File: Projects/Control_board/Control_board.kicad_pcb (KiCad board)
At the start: 2 copper layers, 97.1 x 121.5 mm, 47 parts, among them IC2 PCA9615DPJ, J1 5055780871, J2 43045-0200, J3 43045-0200, J4 43045-0200, J5 43045-0401, J6 RJ45, J8 Conn_01x02, K3 PB114024, Q1 BSS138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

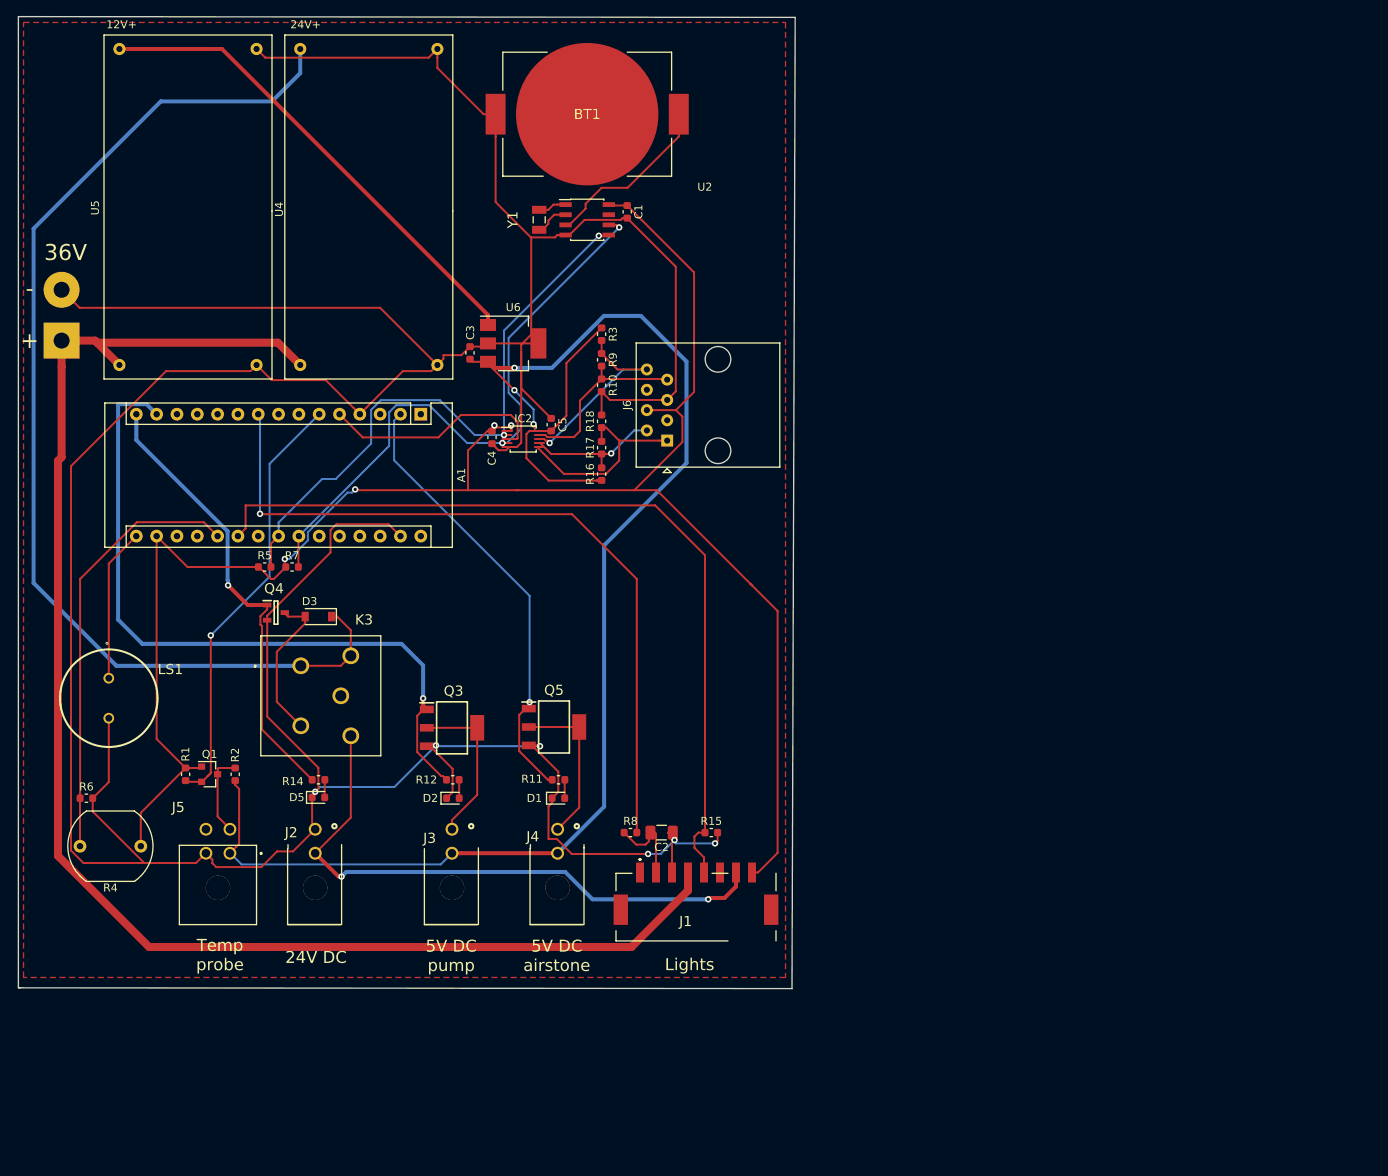
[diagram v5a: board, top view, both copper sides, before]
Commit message: new LED board IS3117... plus sorted out libraries
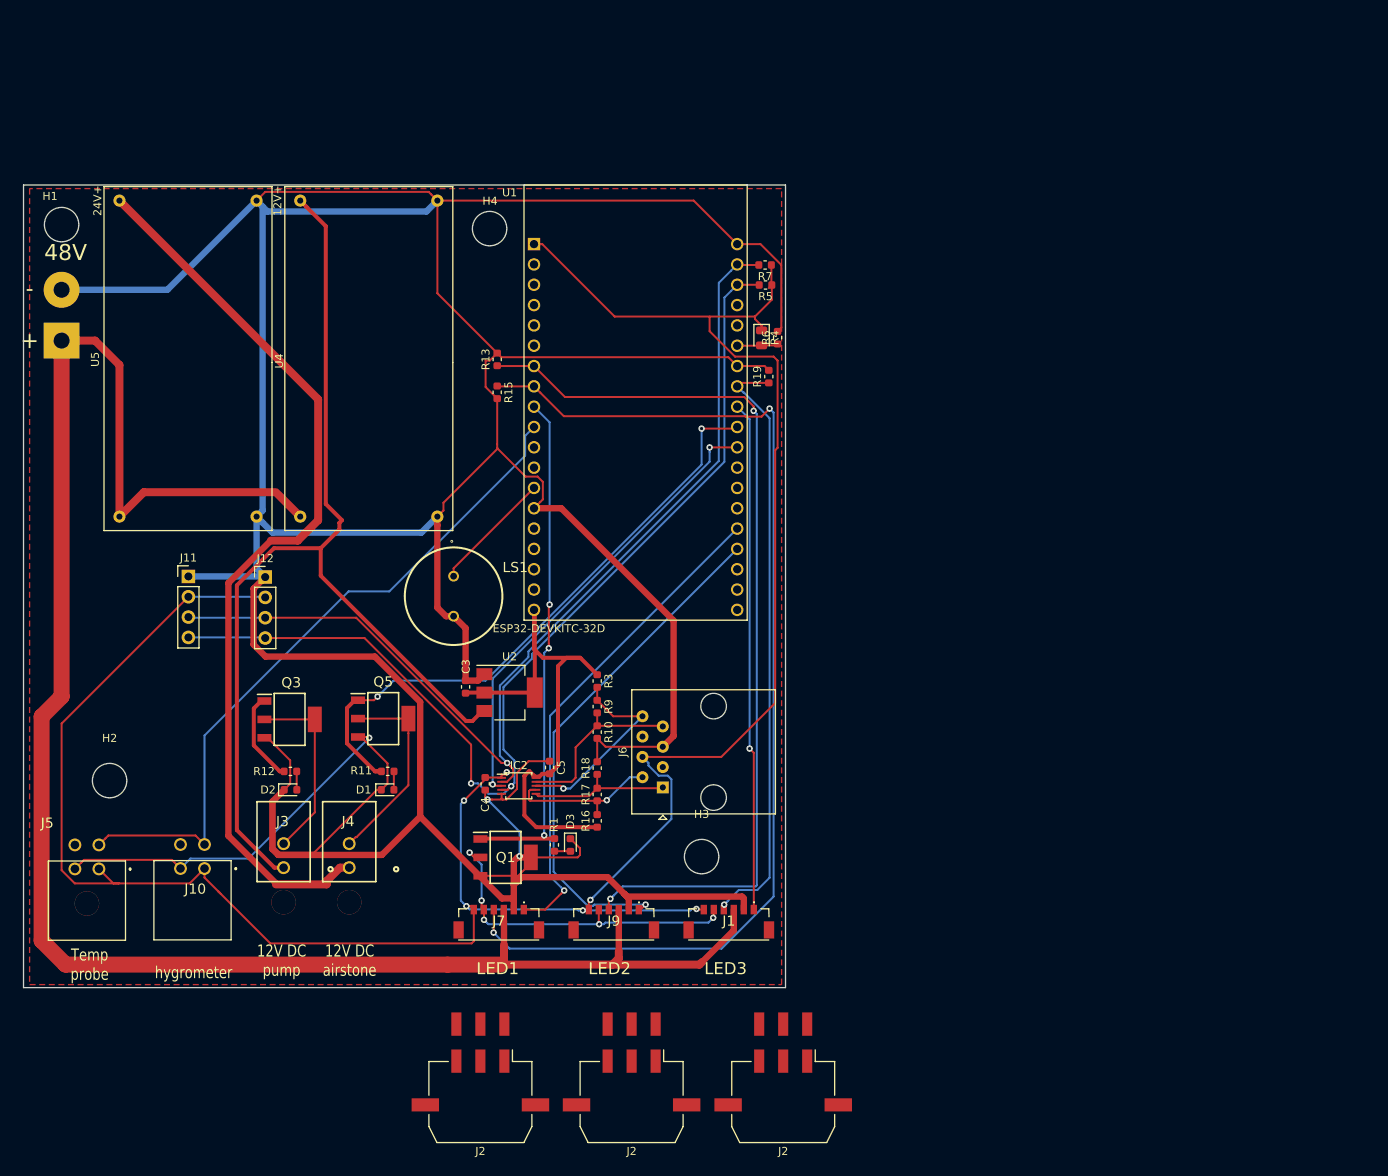
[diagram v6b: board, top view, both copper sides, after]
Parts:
- removed A1: Arduino_Nano_v2.x, Module:Arduino_Nano
- removed BT1: Battery_Cell, SamacSys_Parts:BATHLD001
- removed C1: 0.1uF, Capacitor_SMD:C_0603_1608Metric
- removed C2: 1uF, Capacitor_SMD:C_1206_3216Metric
- removed D5: LED, LED_SMD:LED_0603_1608Metric
- removed the J2 at (115.2, 170.4)
- removed K3: PB114024, SamacSys_Parts:PB114024
- removed Q4: PDTD113ET,215, SamacSys_Parts:SOT95P230X110-3N
- removed R14: 1k, Resistor_SMD:R_0603_1608Metric
- removed R2: 10k, Resistor_SMD:R_0603_1608Metric
- removed R8: 10K, Resistor_SMD:R_0603_1608Metric
- removed U6: TC1262-50, Package_TO_SOT_SMD:SOT-223-3_TabPin2
- removed Y1: Crystal, SamacSys_Parts:FC135327680KAAG0
- added H1: MountingHole, MountingHole:MountingHole_4.3mm_M4, F.Cu at (83.5, 87.5)
- added H2: MountingHole, MountingHole:MountingHole_4.3mm_M4, F.Cu at (89.5, 157.0)
- added H3: MountingHole, MountingHole:MountingHole_4.3mm_M4, F.Cu at (163.5, 166.5)
- added H4: MountingHole, MountingHole:MountingHole_4.3mm_M4, F.Cu at (137.0, 88.0)
- added J10: 43045-0401, SamacSys_Parts:430450401, F.Cu at (100.2, 170.9)
- added J11: Conn_01x04, Connector_PinHeader_2.54mm:PinHeader_1x04_P2.54mm_Vertical, F.Cu at (99.3, 131.5)
- added J12: Conn_01x04, Connector_PinHeader_2.54mm:PinHeader_1x04_P2.54mm_Vertical, F.Cu at (109.0, 131.6)
- added J2: 43045-0609, Connector_Molex:Molex_Micro-Fit_3.0_43045-0610_2x03-1MP_P3.00mm_Horizontal, F.Cu at (173.7, 189.8)
- added J2: 43045-0609, Connector_Molex:Molex_Micro-Fit_3.0_43045-0610_2x03-1MP_P3.00mm_Horizontal, F.Cu at (154.8, 189.8)
- added J2: 43045-0609, Connector_Molex:Molex_Micro-Fit_3.0_43045-0610_2x03-1MP_P3.00mm_Horizontal, F.Cu at (135.8, 189.8)
- added J7: 505567-0681, SamacSys_Parts:5055670681, F.Cu at (138.2, 174.6)
- added J9: 505567-0681, SamacSys_Parts:5055670681, F.Cu at (152.5, 174.6)
- added R13: 10K, Resistor_SMD:R_0603_1608Metric, F.Cu at (137.9, 104.3)
- added R19: 10K, Resistor_SMD:R_0603_1608Metric, F.Cu at (171.9, 106.5)
- added U1: ESP32-DEVKITC-32D, ESP32-DEVKITC-32D:MODULE_ESP32-DEVKITC-32D, F.Cu at (155.2, 109.7)
- D3: value MBR0520 -> LED; footprint Diode_SMD:D_SOD-123 -> LED_SMD:LED_0603_1608Metric
- J1: value 5055780871 -> 505567-0681; footprint footprints:5055780871 -> SamacSys_Parts:5055670681
- J3, J4: footprint Kicad_mylib:Molex_43045-0200 -> 43045-0200
- Q1: value BSS138 -> BSP75N; footprint Package_TO_SOT_SMD:SOT-23 -> SOT230P700X180-4N
- R1: value 10k -> 1k
- R4: footprint OptoDevice:R_LDR_10x8.5mm_P7.6mm_Vertical -> LED_SMD:LED_0805_2012Metric
- U2: value DS1307Z+ -> NCP1117-5.0_SOT223; footprint Package_SO:SOIC-8_3.9x4.9mm_P1.27mm -> Package_TO_SOT_SMD:SOT-223-3_TabPin2
- moved R6 103.8 mm to (173.0, 101.6), turned to 90 degrees
- moved R4 100.3 mm to (171.0, 101.7), turned to 270 degrees
- moved R5 71.8 mm to (171.5, 95.0), turned to 180 degrees
- moved R7 70.1 mm to (171.4, 92.5), turned to 180 degrees
- moved R15 61.2 mm to (137.9, 108.5), turned to 270 degrees
- moved U2 59.9 mm to (139.5, 146.0)
- moved R1 46.9 mm to (145.1, 165.0)
- moved LS1 44.9 mm to (132.5, 133.9)
- moved IC2 43.4 mm to (140.7, 157.7)
- moved R17 43.4 mm to (150.4, 158.7)
- moved R3 43.4 mm to (150.4, 144.6)
- moved J6 43.4 mm to (158.7, 157.8)
- moved R10 43.4 mm to (150.4, 150.9)
- moved R16 43.4 mm to (150.4, 162.0)
- moved R18 43.4 mm to (150.4, 155.4)
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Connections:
- D3 pad 1: +24V -> GND
- IC2 pad 2: Net-(A1-Pad23) -> /SDA
- IC2 pad 4: Net-(A1-Pad24) -> /SCL
- J1 pad 1: (no net) -> /ADJ_LED1
- J1 pad 2: /ADJ_LED -> GND
- J1 pad 3: GND -> +48V
- J1 pad 4: +36V -> /NTC_1
- J1 pad 5: /NTC -> /48V_Fan
- J1 pad 6: (no net) -> +3V3
- J1 pad 7: /12V_Fan -> (no net)
- J1 pad 8: +3V3 -> (no net)
- J3 pad 1: +5V -> +12V
- J4 pad 1: +5V -> +24V
- J5 pad 1: +5V -> +3V3
- J5 pad 3: /temp_data_5V -> /1-Wire
- J8 pad 1: +36V -> +48V
- LS1 pad 1: Net-(A1-Pad16) -> /buzzer
- Q1 pad 1: +3V3 -> /fan
- Q1 pad 2: /Temp_data_3V3 -> /48V_Fan
- Q1 pad 3: /temp_data_5V -> GND
- R1 pad 1: +3V3 -> /fan
- R1 pad 2: /Temp_data_3V3 -> Net-(D3-Pad2)
- R15 pad 1: /NTC -> /NTC_2
- R5 pad 2: Net-(A1-Pad23) -> /SCL
- R7 pad 2: Net-(A1-Pad24) -> /SDA
- U2 pad 1: Net-(U2-Pad1) -> GND
- U2 pad 2: Net-(U2-Pad2) -> +5V
- U2 pad 3: Net-(BT1-Pad1) -> +12V
- U4 pad 1: +36V -> +48V
- U4 pad 4: +24V -> +12V
- U5 pad 1: +36V -> +48V
- U5 pad 4: +12V -> +24V
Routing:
- net +48V: track 0.00 -> 239.2 mm
- net +36V: track 188.3 -> 0.00 mm
- net /NTC_2: track 0.00 -> 138.9 mm, vias 0 -> 2
- net GND: track 509.0 -> 642.1 mm, vias 6 -> 3
- net /SCL: track 0.00 -> 131.4 mm, vias 0 -> 2
- net /SDA: track 0.00 -> 128.8 mm, vias 0 -> 1
- net +5V: track 195.9 -> 69.2 mm, vias 3 -> 0
- net /NTC_3: track 0.00 -> 114.6 mm, vias 0 -> 2
- net /NTC: track 105.4 -> 0.00 mm
- net /ADJ: track 94.7 -> 0.00 mm, vias 1 -> 0
- net /1-Wire: track 0.00 -> 86.4 mm
- net /pump: track 89.6 -> 11.5 mm, vias 1 -> 0
- net Net-(A1-Pad24): track 77.7 -> 0.00 mm, vias 2 -> 0
- net Net-(A1-Pad23): track 76.8 -> 0.00 mm, vias 2 -> 0
- net +3V3: track 234.2 -> 310.2 mm, vias 4 -> 6
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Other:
- board size 97.1 x 121.5 mm -> 95.3 x 100.3 mm
- net class 36volt removed
- net class 48volt added: clearance 0.4, trace_width 1, via_dia 0.8, via_drill 0.4
- net class Power: trace_width 1 -> 0.8
- board text added: "12V DC airstone"
- board text added: "12V DC pump"
- board text added: "48V"
- board text added: "LED1"
- board text added: "LED2"
- board text added: "LED3"
- board text added: "hygrometer"
- board text removed: "24V DC"
- board text removed: "36V"
- board text removed: "5V DC airstone"
- board text removed: "5V DC pump"
- board text removed: "Lights"

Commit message: files after harddrive restore
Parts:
- removed the J2 at (173.7, 189.8)
- removed the J2 at (154.8, 189.8)
- removed the J2 at (135.8, 189.8)
- removed J9: 505567-0681, SamacSys_Parts:5055670681
- removed U5: DCDC_lm2596, Kicad_mylib:LM2596_module
- added C1: 100nF, Capacitor_SMD:C_0603_1608Metric, F.Cu at (137.0, 154.0)
- added C2: 100nF, Capacitor_SMD:C_0603_1608Metric, F.Cu at (151.2, 154.0)
- added C6: 100nF, Capacitor_SMD:C_0603_1608Metric, F.Cu at (166.2, 153.8)
- added C7: 100nF, Capacitor_SMD:C_0603_1608Metric, F.Cu at (174.0, 124.2)
- added D4: SMF5.0A, Diode_SMD:D_SOD-123F, F.Cu at (161.6, 157.2)
- added D5: SMF5.0A, Diode_SMD:D_SOD-123F, F.Cu at (146.2, 157.2)
- added D6: SMF5.0A, Diode_SMD:D_SOD-123F, F.Cu at (132.0, 157.2)
- added D7: SMF5.0A, Diode_SMD:D_SOD-123F, F.Cu at (137.4, 157.2)
- added D8: SMF5.0A, Diode_SMD:D_SOD-123F, F.Cu at (151.4, 157.2)
- added D9: SMF5.0A, Diode_SMD:D_SOD-123F, F.Cu at (166.6, 157.2)
- added IC1: VN7050ASTR, SamacSys_Parts:SOIC127P600X175-8N, F.Cu at (134.0, 146.5)
- added IC3: PSSI2021SAY,115, SamacSys_Parts:SOT65P210X100-5N, F.Cu at (100.0, 154.5)
- added J13: Conn_01x01_Female, Connector_PinHeader_1.00mm:PinHeader_1x01_P1.00mm_Horizontal, F.Cu at (170.8, 120.5)
- added J2: 66200621022, SamacSys_Parts:66200621022, F.Cu at (153.0, 167.8)
- added Q2: BSS138-Transistor_FET, Package_TO_SOT_SMD:SOT-23, F.Cu at (136.6, 125.4)
- added R14: 100, Resistor_SMD:R_0603_1608Metric, F.Cu at (151.2, 151.0)
- added R2: 10K, Resistor_SMD:R_0603_1608Metric, F.Cu at (136.8, 121.6)
- added R20: 100, Resistor_SMD:R_0603_1608Metric, F.Cu at (166.2, 151.0)
- added R21: 100, Resistor_SMD:R_0603_1608Metric, F.Cu at (171.0, 124.2)
- added R22: 4.7k, Resistor_SMD:R_0603_1608Metric, F.Cu at (98.5, 150.8)
- added R23: 15k, Resistor_SMD:R_0603_1608Metric, F.Cu at (138.0, 142.8)
- added R24: 39k, Resistor_SMD:R_0603_1608Metric, F.Cu at (96.2, 154.5)
- added R25: 10k, Resistor_SMD:R_0603_1608Metric, F.Cu at (102.8, 154.5)
- added R8: 100, Resistor_SMD:R_0603_1608Metric, F.Cu at (137.0, 151.0)
- J1, J7: value 505567-0681 -> 66200621022; footprint SamacSys_Parts:5055670681 -> SamacSys_Parts:66200621022
- J3, J4: footprint 43045-0200 -> footprints:43045-0200
- Q1: value BSP75N -> Q_NMOS_GSD; footprint SOT230P700X180-4N -> Package_TO_SOT_SMD:SOT-23
- moved J6 81.4 mm to (103.8, 97.6), turned to 180 degrees
- moved R3 71.3 mm to (90.5, 105.8), turned to 0 degrees
- moved R9 70.5 mm to (93.8, 105.8), turned to 0 degrees
- moved R16 70.4 mm to (108.0, 105.8), turned to 180 degrees
- moved R10 70.0 mm to (96.9, 105.8), turned to 0 degrees
- moved R17 69.9 mm to (104.7, 105.8), turned to 180 degrees
- moved R18 69.8 mm to (101.4, 105.8), turned to 180 degrees
- moved C5 61.3 mm to (101.4, 111.8), turned to 0 degrees
- moved IC2 56.0 mm to (103.7, 115.6), turned to 90 degrees
- moved U2 55.8 mm to (92.5, 116.0), turned to 90 degrees
- moved C4 50.1 mm to (103.4, 119.8), turned to 0 degrees
- moved Q1 42.2 mm to (97.2, 160.2)
- moved J7 32.9 mm to (170.4, 167.8), turned to 0 degrees
- moved J1 32.6 mm to (135.0, 167.8), turned to 0 degrees
- moved R6 26.6 mm to (174.0, 128.2), turned to 270 degrees
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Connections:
- J1 pad 1: /ADJ_LED1 -> GND
- J1 pad 2: GND -> /ADJ_LED1
- J1 pad 3: +48V -> /NTC_1
- J1 pad 4: /NTC_1 -> +48V
- J1 pad 5: /48V_Fan -> /12V_Fan
- J10 pad 3: /1-Wire -> Net-(J10-Pad3)
- J4 pad 1: +24V -> +12V
- J5 pad 3: /1-Wire -> Net-(J10-Pad3)
- J7 pad 1: /ADJ_LED2 -> GND
- J7 pad 2: GND -> /ADJ_LED3
- J7 pad 3: +48V -> /NTC_3
- J7 pad 4: /NTC_2 -> +48V
- J7 pad 5: /48V_Fan -> /12V_Fan
- LS1 pad 1: /buzzer -> +3V3
- LS1 pad 2: GND -> Net-(LS1-Pad2)
- Q1 pad 1: /fan -> Net-(IC3-Pad2)
- Q1 pad 2: /48V_Fan -> Net-(J10-Pad3)
- Q1 pad 3: GND -> /1-Wire
- R4 pad 2: /LDR -> Net-(C7-Pad1)
- R6 pad 1: /LDR -> Net-(C7-Pad1)
- U1 pad 11: (no net) -> /EN
- U1 pad 15: (no net) -> /pump
- U1 pad 25: /LDR -> (no net)
- U1 pad 28: /ADJ_LED1 -> Net-(R8-Pad2)
- U1 pad 30: /EN -> (no net)
- U1 pad 32: (no net) -> /Touch
- U1 pad 33: (no net) -> /LDR
- U1 pad 34: /ADJ_LED2 -> Net-(R14-Pad2)
- U1 pad 35: /ADJ_LED3 -> Net-(R20-Pad2)
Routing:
- net +24V: track 115.1 -> 0.00 mm
- net +5V: track 69.2 -> 159.5 mm, vias 0 -> 2
- net GND: track 642.1 -> 725.5 mm, vias 3 -> 7
- net /12V_Fan: track 0.00 -> 62.6 mm, vias 0 -> 1
- net /NTC_1: track 75.0 -> 132.7 mm, vias 1 -> 0
- net Net-(R8-Pad2): track 0.00 -> 56.9 mm, vias 0 -> 1
- net /ADJ_LED3: track 64.3 -> 17.8 mm, vias 1 -> 0
- net /ADJ_LED1: track 63.7 -> 18.6 mm, vias 1 -> 0
- net /pump: track 11.5 -> 54.6 mm, vias 0 -> 1
- net /48V_Fan: track 42.9 -> 0.00 mm, vias 5 -> 0
- net /NTC_3: track 114.6 -> 76.3 mm, vias 2 -> 1
- net /ADJ_LED2: track 61.7 -> 27.0 mm, vias 1 -> 0
- net Net-(R14-Pad2): track 0.00 -> 32.2 mm, vias 0 -> 1
- net +12V: track 129.4 -> 158.5 mm
- net Net-(J10-Pad3): track 0.00 -> 28.5 mm
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- added copper zone on B.Cu, net GND
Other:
- board size 95.3 x 100.3 mm -> 99.5 x 100.4 mm
